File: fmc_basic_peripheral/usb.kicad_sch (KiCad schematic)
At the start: 15 parts, among them J3 USB_C_Receptacle, U12 TPD4E02B04DQA, U2 STUSB03EQR, U5 AIP74LVC1T45GB236TR

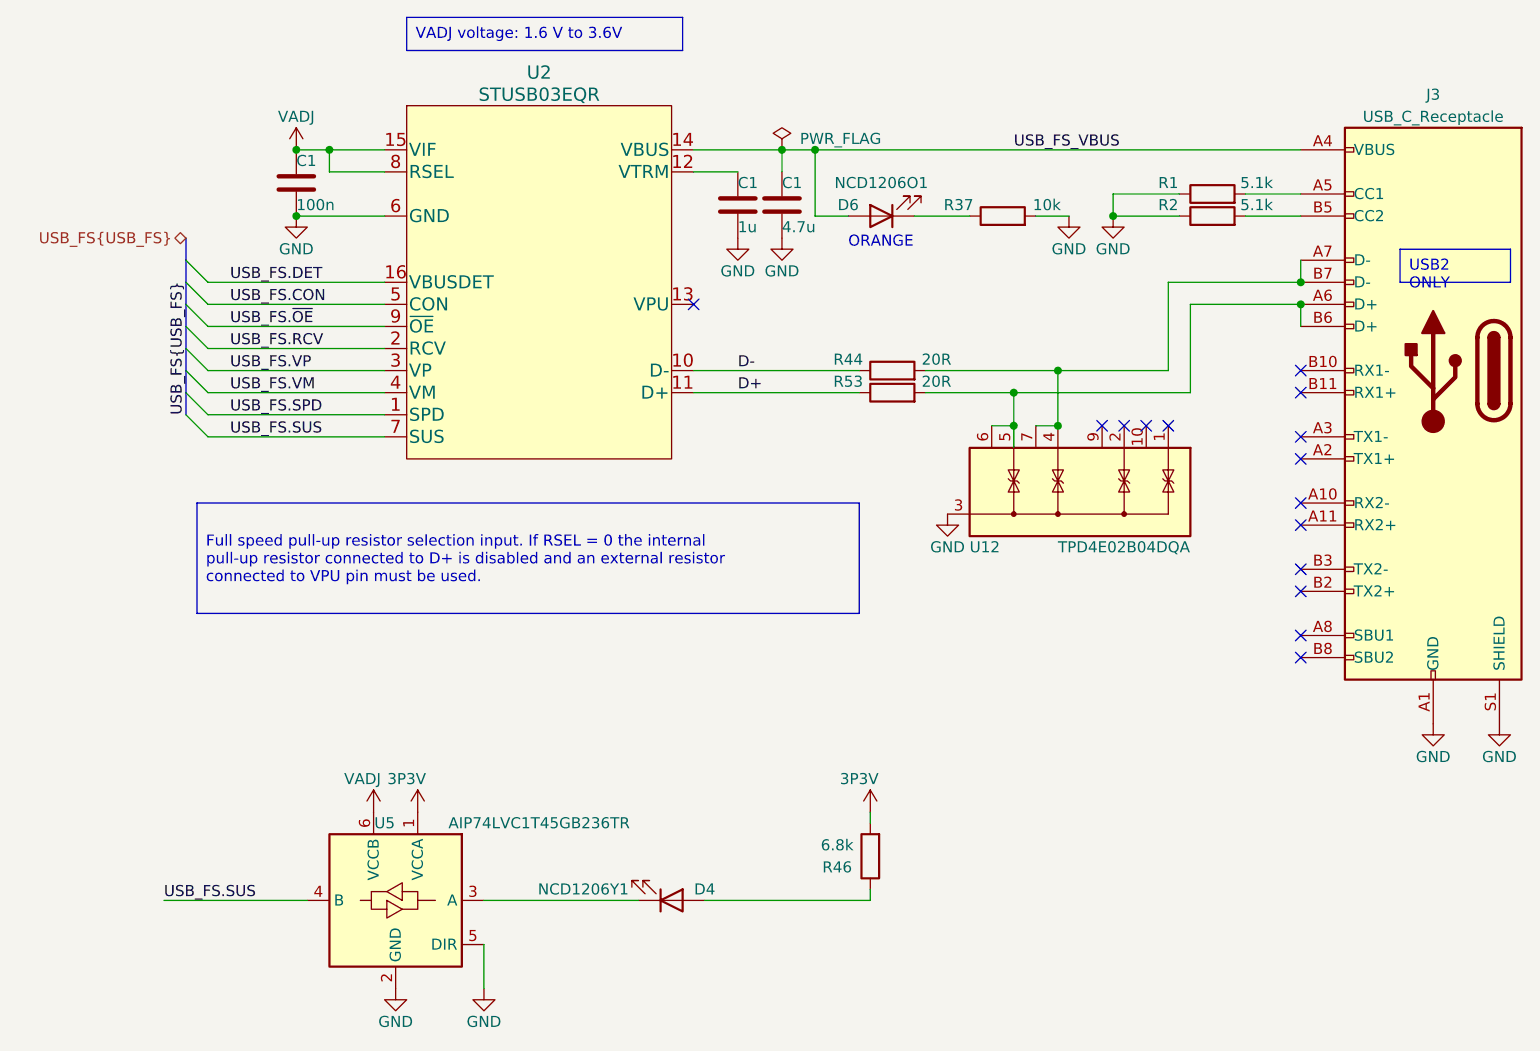
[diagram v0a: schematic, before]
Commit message: fmc_basic_peripheral: Migrate to kicad8
- Migrate schematics to kicad8
- Migrate PCB to kicad8
- Clean ERC
- Clean LVS and DRC

Signed-off-by: Huang Rui <vowstar@gmail.com>
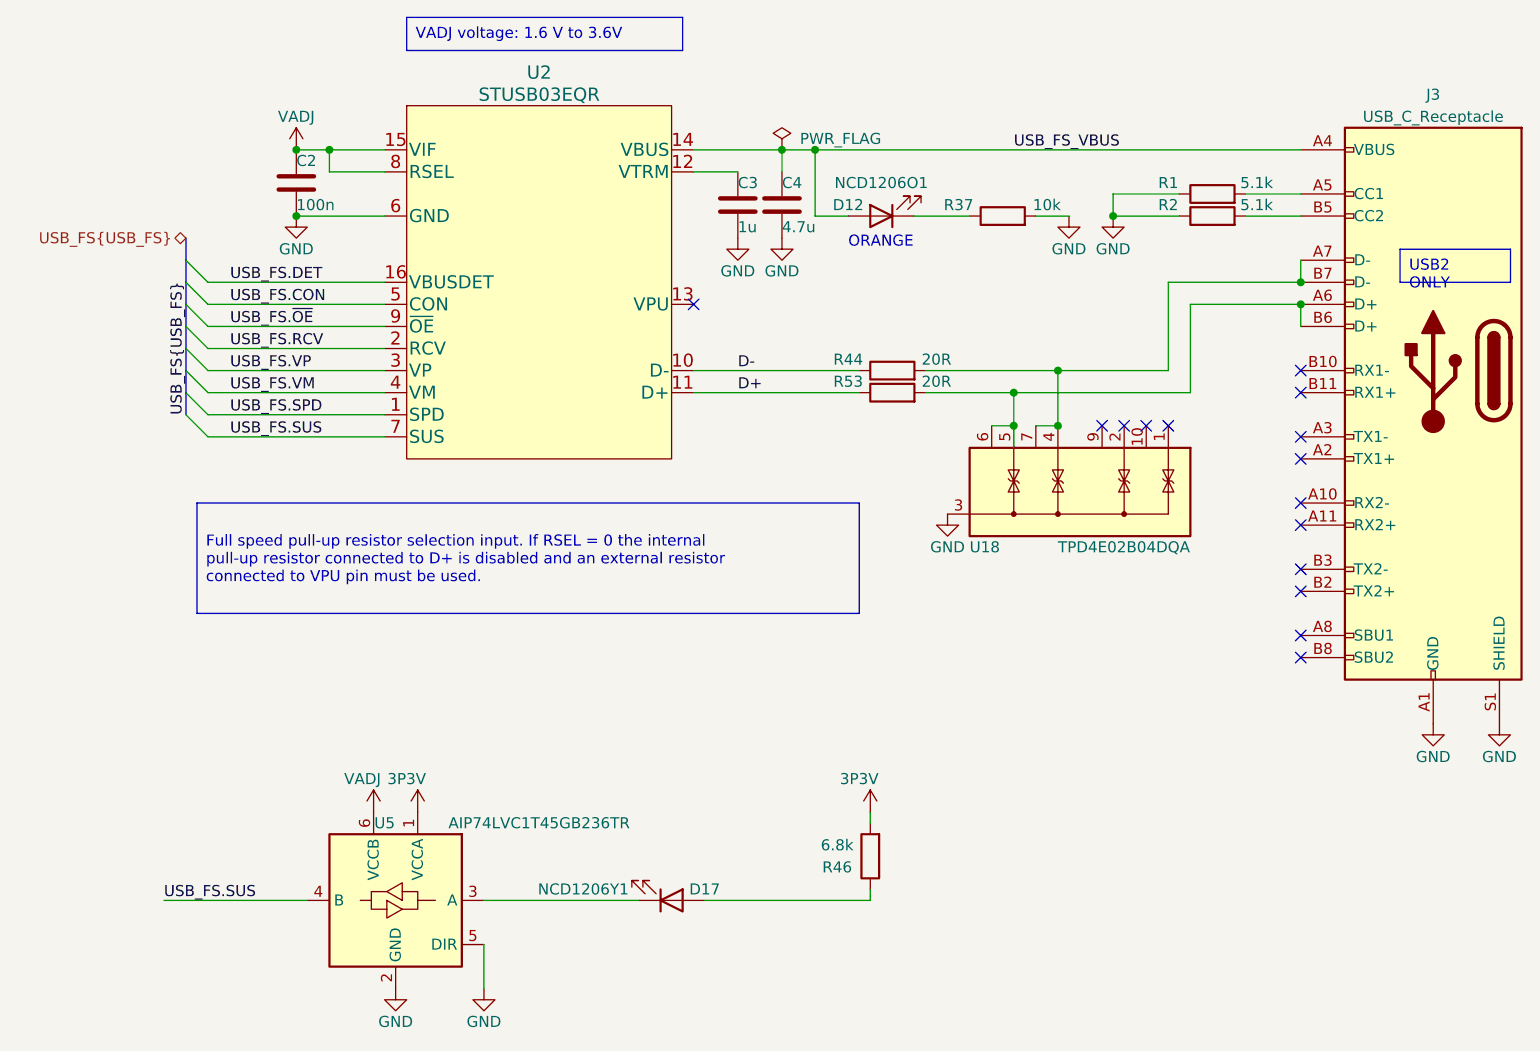
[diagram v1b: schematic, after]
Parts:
- renumbered C1 to C2, C1 to C3, C1 to C4, D6 to D12, D4 to D17, U12 to U18

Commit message: fmc_basic_peripheral: update SOT-23-5 footprint and fix DRC
Signed-off-by: Huang Rui <vowstar@gmail.com>
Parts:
- U5: footprint Package_TO_SOT_SMD:SOT-23-6 -> CHIPSAlliance_Package_TO_SOT_SMD:SOT-23-6
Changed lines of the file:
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@@
 			)
 		)
-		(property "Footprint" "Package_TO_SOT_SMD:SOT-23-6"
+		(property "Footprint" "CHIPSAlliance_Package_TO_SOT_SMD:SOT-23-6"
 			(at 82.55 151.13 0)
 			(effects
